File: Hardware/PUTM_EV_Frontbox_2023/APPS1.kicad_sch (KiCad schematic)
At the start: 23 parts, among them U15 MCP6001, U9 MCP6N11-005

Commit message: Merged branch new_apps
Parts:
- renumbered C2 to C49, C22 to C50, C27 to C51, C30 to C52, C32 to C53, C34 to C54, D7 to D9, JP1 to JP3, R7 to R67, R8 to R68, R32 to R69, R34 to R70, R36 to R71, R37 to R72, R53 to R73, R55 to R74, RV1 to RV6, TP6 to TP26, TP7 to TP27, TP10 to TP28, TP12 to TP29, U9 to U18, U15 to U21
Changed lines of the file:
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@@
   (symbol (lib_id "Connector:TestPoint") (at 173.99 99.695 0) (unit 1)
     (in_bom yes) (on_board yes) (dnp no)
-    (property "Reference" "TP10" (at 172.72 93.345 0)
+    (property "Reference" "TP28" (at 172.72 93.345 0)
       (effects (font (size 1.27 1.27)) (justify left))
     )
@@
   (symbol (lib_id "Device:R_Small") (at 83.82 114.935 0) (unit 1)
     (in_bom yes) (on_board yes) (dnp no)
-    (property "Reference" "R8" (at 85.3186 113.7666 0)
+    (property "Reference" "R68" (at 85.3186 113.7666 0)
       (effects (font (size 1.27 1.27)) (justify left))
     )
@@
   (symbol (lib_id "Device:R_Small") (at 156.21 90.805 180) (unit 1)
     (in_bom yes) (on_board yes) (dnp no)
-    (property "Reference" "R34" (at 158.75 92.075 90)
+    (property "Reference" "R70" (at 158.75 92.075 90)
       (effects (font (size 1.27 1.27)))
     )
@@
   (symbol (lib_id "Device:R_Small") (at 166.37 103.505 180) (unit 1)
     (in_bom yes) (on_board yes) (dnp no)
-    (property "Reference" "R36" (at 163.83 103.505 90)
+    (property "Reference" "R71" (at 163.83 103.505 90)
       (effects (font (size 1.27 1.27)))
     )
@@
   (symbol (lib_id "power:GND") (at 203.2 111.125 0) (unit 1)
     (in_bom yes) (on_board yes) (dnp no)
-    (property "Reference" "#PWR0112" (at 203.2 117.475 0)
+    (property "Reference" "#PWR0124" (at 203.2 117.475 0)
       (effects (font (size 1.27 1.27)) hide)
     )
@@
   (symbol (lib_id "Device:R_Small") (at 184.15 99.695 90) (unit 1)
     (in_bom yes) (on_board yes) (dnp no)
-    (property "Reference" "R53" (at 184.15 97.155 90)
+    (property "Reference" "R73" (at 184.15 97.155 90)
       (effects (font (size 1.27 1.27)))
     )
@@
   (symbol (lib_id "power:GND") (at 166.37 116.205 0) (unit 1)
     (in_bom yes) (on_board yes) (dnp no)
-    (property "Reference" "#PWR0109" (at 166.37 122.555 0)
+    (property "Reference" "#PWR0123" (at 166.37 122.555 0)
       (effects (font (size 1.27 1.27)) hide)
     )
@@
   (symbol (lib_id "Connector:TestPoint") (at 140.97 97.155 0) (unit 1)
     (in_bom yes) (on_board yes) (dnp no)
-    (property "Reference" "TP6" (at 139.7 90.805 0)
+    (property "Reference" "TP26" (at 139.7 90.805 0)
       (effects (font (size 1.27 1.27)) (justify left))
     )
@@
   (symbol (lib_id "power:GND") (at 60.96 118.745 0) (unit 1)
     (in_bom yes) (on_board yes) (dnp no)
-    (property "Reference" "#PWR023" (at 60.96 125.095 0)
+    (property "Reference" "#PWR0105" (at 60.96 125.095 0)
       (effects (font (size 1.27 1.27)) hide)
     )
@@
   (symbol (lib_id "Device:C_Small") (at 55.88 112.395 0) (unit 1)
     (in_bom yes) (on_board yes) (dnp no)
-    (property "Reference" "C2" (at 58.42 111.7663 0)
+    (property "Reference" "C49" (at 58.42 111.7663 0)
       (effects (font (size 1.27 1.27)) (justify left))
     )
@@
   (symbol (lib_id "Device:C_Small") (at 209.55 80.645 90) (unit 1)
     (in_bom yes) (on_board yes) (dnp no)
-    (property "Reference" "C34" (at 207.6513 78.105 90)
+    (property "Reference" "C54" (at 207.6513 78.105 90)
       (effects (font (size 1.27 1.27)) (justify left))
     )
@@
   (symbol (lib_id "Device:R_Small") (at 194.31 99.695 90) (unit 1)
     (in_bom yes) (on_board yes) (dnp no)
-    (property "Reference" "R55" (at 194.31 97.155 90)
+    (property "Reference" "R74" (at 194.31 97.155 90)
       (effects (font (size 1.27 1.27)))
     )
@@
   (symbol (lib_id "Device:R_Small") (at 106.68 84.455 0) (unit 1)
     (in_bom yes) (on_board yes) (dnp no)
-    (property "Reference" "R32" (at 108.1786 83.2866 0)
+    (property "Reference" "R69" (at 108.1786 83.2866 0)
       (effects (font (size 1.27 1.27)) (justify left))
     )
@@
   (symbol (lib_id "Connector:TestPoint") (at 232.41 102.235 0) (unit 1)
     (in_bom yes) (on_board yes) (dnp no)
-    (property "Reference" "TP12" (at 231.14 95.885 0)
+    (property "Reference" "TP29" (at 231.14 95.885 0)
       (effects (font (size 1.27 1.27)) (justify left))
     )
@@
   (symbol (lib_id "Jumper:SolderJumper_3_Bridged12") (at 106.68 108.585 180) (unit 1)
     (in_bom yes) (on_board yes) (dnp no)
-    (property "Reference" "JP1" (at 111.76 106.045 0)
+    (property "Reference" "JP3" (at 111.76 106.045 0)
       (effects (font (size 1.27 1.27)))
     )
@@
   (symbol (lib_id "power:GND") (at 106.68 89.535 0) (unit 1)
     (in_bom yes) (on_board yes) (dnp no)
-    (property "Reference" "#PWR094" (at 106.68 95.885 0)
+    (property "Reference" "#PWR0118" (at 106.68 95.885 0)
       (effects (font (size 1.27 1.27)) hide)
     )
@@
   (symbol (lib_id "power:GND") (at 153.67 108.585 0) (unit 1)
     (in_bom yes) (on_board yes) (dnp no)
-    (property "Reference" "#PWR0107" (at 153.67 114.935 0)
+    (property "Reference" "#PWR0122" (at 153.67 114.935 0)
       (effects (font (size 1.27 1.27)) hide)
     )
@@
   (symbol (lib_id "Device:C_Small") (at 115.57 114.935 0) (unit 1)
     (in_bom yes) (on_board yes) (dnp yes)
-    (property "Reference" "C30" (at 118.11 113.665 0)
+    (property "Reference" "C52" (at 118.11 113.665 0)
       (effects (font (size 1.27 1.27)) (justify left))
     )
@@
   (symbol (lib_id "Device:C_Small") (at 66.04 112.395 0) (unit 1)
     (in_bom yes) (on_board yes) (dnp no)
-    (property "Reference" "C22" (at 68.58 111.7663 0)
+    (property "Reference" "C50" (at 68.58 111.7663 0)
       (effects (font (size 1.27 1.27)) (justify left))
     )
@@
   (symbol (lib_id "Device:R_Small") (at 83.82 102.235 0) (unit 1)
     (in_bom yes) (on_board yes) (dnp no)
-    (property "Reference" "R7" (at 85.3186 101.0666 0)
+    (property "Reference" "R67" (at 85.3186 101.0666 0)
       (effects (font (size 1.27 1.27)) (justify left))
     )
@@
   (symbol (lib_id "Device:C_Small") (at 93.98 114.935 0) (unit 1)
     (in_bom yes) (on_board yes) (dnp no)
-    (property "Reference" "C27" (at 96.52 113.665 0)
+    (property "Reference" "C51" (at 96.52 113.665 0)
       (effects (font (size 1.27 1.27)) (justify left))
     )
@@
   (symbol (lib_id "power:GND") (at 115.57 118.745 0) (unit 1)
     (in_bom yes) (on_board yes) (dnp no)
-    (property "Reference" "#PWR096" (at 115.57 125.095 0)
+    (property "Reference" "#PWR0119" (at 115.57 125.095 0)
       (effects (font (size 1.27 1.27)) hide)
     )
@@
   (symbol (lib_id "power:GND") (at 93.98 118.745 0) (unit 1)
     (in_bom yes) (on_board yes) (dnp no)
-    (property "Reference" "#PWR034" (at 93.98 125.095 0)
+    (property "Reference" "#PWR0117" (at 93.98 125.095 0)
       (effects (font (size 1.27 1.27)) hide)
     )
@@
   (symbol (lib_id "Device:R_Small") (at 166.37 111.125 180) (unit 1)
     (in_bom yes) (on_board yes) (dnp no)
-    (property "Reference" "R37" (at 163.83 111.125 90)
+    (property "Reference" "R72" (at 163.83 111.125 90)
       (effects (font (size 1.27 1.27)))
     )
@@
   (symbol (lib_id "power:GND") (at 83.82 118.745 0) (unit 1)
     (in_bom yes) (on_board yes) (dnp no)
-    (property "Reference" "#PWR031" (at 83.82 125.095 0)
+    (property "Reference" "#PWR0116" (at 83.82 125.095 0)
       (effects (font (size 1.27 1.27)) hide)
     )
@@
   (symbol (lib_id "Device:C_Small") (at 203.2 106.045 0) (mirror y) (unit 1)
     (in_bom yes) (on_board yes) (dnp no)
-    (property "Reference" "C32" (at 200.66 105.4163 0)
+    (property "Reference" "C53" (at 200.66 105.4163 0)
       (effects (font (size 1.27 1.27)) (justify left))
     )
@@
   (symbol (lib_id "Connector:TestPoint") (at 140.97 102.235 180) (unit 1)
     (in_bom yes) (on_board yes) (dnp no)
-    (property "Reference" "TP7" (at 139.7 108.585 0)
+    (property "Reference" "TP27" (at 139.7 108.585 0)
       (effects (font (size 1.27 1.27)) (justify right))
     )
@@
   (symbol (lib_id "power:GND") (at 116.84 89.535 0) (unit 1)
     (in_bom yes) (on_board yes) (dnp no)
-    (property "Reference" "#PWR098" (at 116.84 95.885 0)
+    (property "Reference" "#PWR0121" (at 116.84 95.885 0)
       (effects (font (size 1.27 1.27)) hide)
     )
@@
   (symbol (lib_id "power:GND") (at 217.17 111.125 0) (unit 1)
     (in_bom yes) (on_board yes) (dnp no)
-    (property "Reference" "#PWR0114" (at 217.17 117.475 0)
+    (property "Reference" "#PWR0125" (at 217.17 117.475 0)
       (effects (font (size 1.27 1.27)) hide)
     )
@@
   (symbol (lib_id "Amplifier_Operational:MCP6001-OT") (at 219.71 102.235 0) (unit 1)
     (in_bom yes) (on_board yes) (dnp no)
-    (property "Reference" "U15" (at 222.25 98.8061 0)
+    (property "Reference" "U21" (at 222.25 98.8061 0)
       (effects (font (size 1.27 1.27)))
     )
@@
   (symbol (lib_id "Device:D_TVS") (at 116.84 84.455 90) (unit 1)
     (in_bom yes) (on_board yes) (dnp no) (fields_autoplaced)
-    (property "Reference" "D7" (at 119.38 83.185 90)
+    (property "Reference" "D9" (at 119.38 83.185 90)
       (effects (font (size 1.27 1.27)) (justify right))
     )
@@
   (symbol (lib_id "MCP6N11:MCP6N11") (at 156.21 99.695 0) (unit 1)
     (in_bom yes) (on_board yes) (dnp no)
-    (property "Reference" "U9" (at 160.02 97.155 0)
+    (property "Reference" "U18" (at 160.02 97.155 0)
       (effects (font (size 1.27 1.27)))
     )
@@
   (symbol (lib_id "Device:R_Potentiometer_Small") (at 83.82 108.585 0) (unit 1)
     (in_bom yes) (on_board yes) (dnp no)
-    (property "Reference" "RV1" (at 82.55 106.68 0)
+    (property "Reference" "RV6" (at 82.55 106.68 0)
       (effects (font (size 1.27 1.27)) (justify right))
     )

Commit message: Updated PCB
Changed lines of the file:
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@@
     (stroke (width 0) (type default))
   )
-  (wire (pts (xy 217.17 93.345) (xy 217.17 94.615))
+  (wire (pts (xy 217.17 93.98) (xy 217.17 94.615))
     (stroke (width 0) (type default))
   )
@@
     (effects (font (size 1.27 1.27)) (justify left bottom))
   )
-  (global_label "3V3_POT1" (shape input) (at 217.17 93.345 90) (fields_autoplaced)
+  (global_label "3V3_POT1" (shape input) (at 217.17 93.98 90) (fields_autoplaced)
     (effects (font (size 1.27 1.27)) (justify left))
-    (property "Intersheetrefs" "${INTERSHEET_REFS}" (at 217.17 81.8406 90)
+    (property "Intersheetrefs" "${INTERSHEET_REFS}" (at 217.17 82.4756 90)
       (effects (font (size 1.27 1.27)) (justify left) hide)
     )

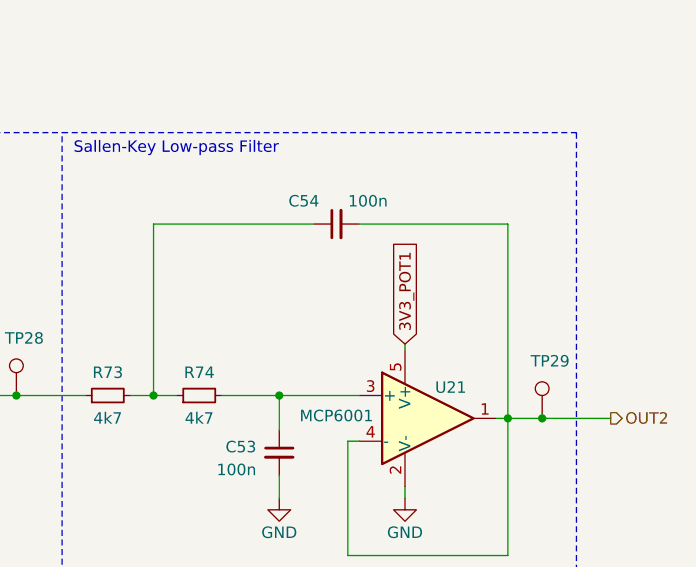
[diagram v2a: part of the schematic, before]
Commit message: Schematic updates
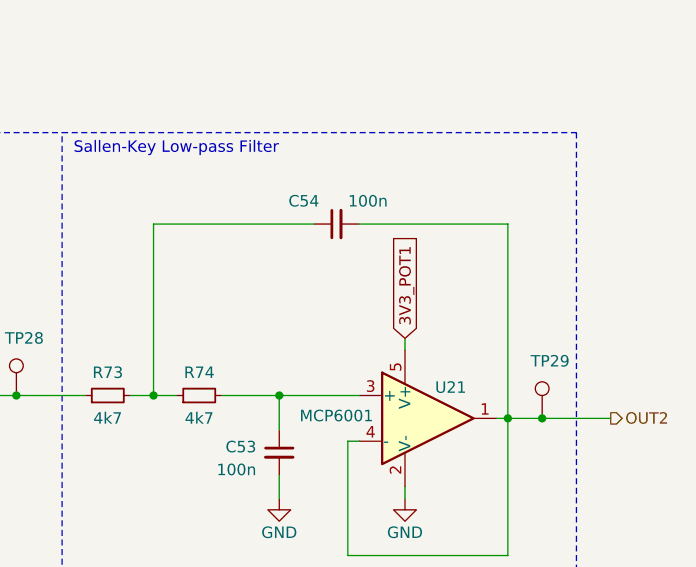
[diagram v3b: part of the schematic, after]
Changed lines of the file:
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@@
     (stroke (width 0) (type default))
   )
-  (wire (pts (xy 217.17 93.98) (xy 217.17 94.615))
+  (wire (pts (xy 217.17 93.345) (xy 217.17 94.615))
     (stroke (width 0) (type default))
   )
@@
     (effects (font (size 1.27 1.27)) (justify left bottom))
   )
-  (global_label "3V3_POT1" (shape input) (at 217.17 93.98 90) (fields_autoplaced)
+  (global_label "3V3_POT1" (shape input) (at 217.17 93.345 90) (fields_autoplaced)
     (effects (font (size 1.27 1.27)) (justify left))
-    (property "Intersheetrefs" "${INTERSHEET_REFS}" (at 217.17 82.4756 90)
+    (property "Intersheetrefs" "${INTERSHEET_REFS}" (at 217.17 81.8406 90)
       (effects (font (size 1.27 1.27)) (justify left) hide)
     )
